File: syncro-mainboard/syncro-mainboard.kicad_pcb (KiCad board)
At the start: 4 copper layers, 78.5 x 59 mm, 146 parts, among them J1 USB_C_Receptacle_USB2.0_16P, J2 Conn_01x03, J3 Conn_ARM_JTAG_SWD_10, J4 Micro_SD_Card_Det1, J5 USB_A, J6 USB_A, J7 USB_A, J8 MikroBUS, J9 Qwiic, Q1 AO3401A, SW1 RESET, SW2 USB BOOT, SW3 SW_USER, U1 MYC-YF135, U10 ECMF02-2AMX6, U11 TPS25200, U2 TS3USB221ARSER, U3 TS3USB221ARSER, U4 ECMF02-2AMX6, U5 FE1.1s, U6 TPS25200, U7 EMIF06-MSD02N16, U8 ECMF02-2AMX6, U9 ECMF02-2AMX6, Y1 12MHz

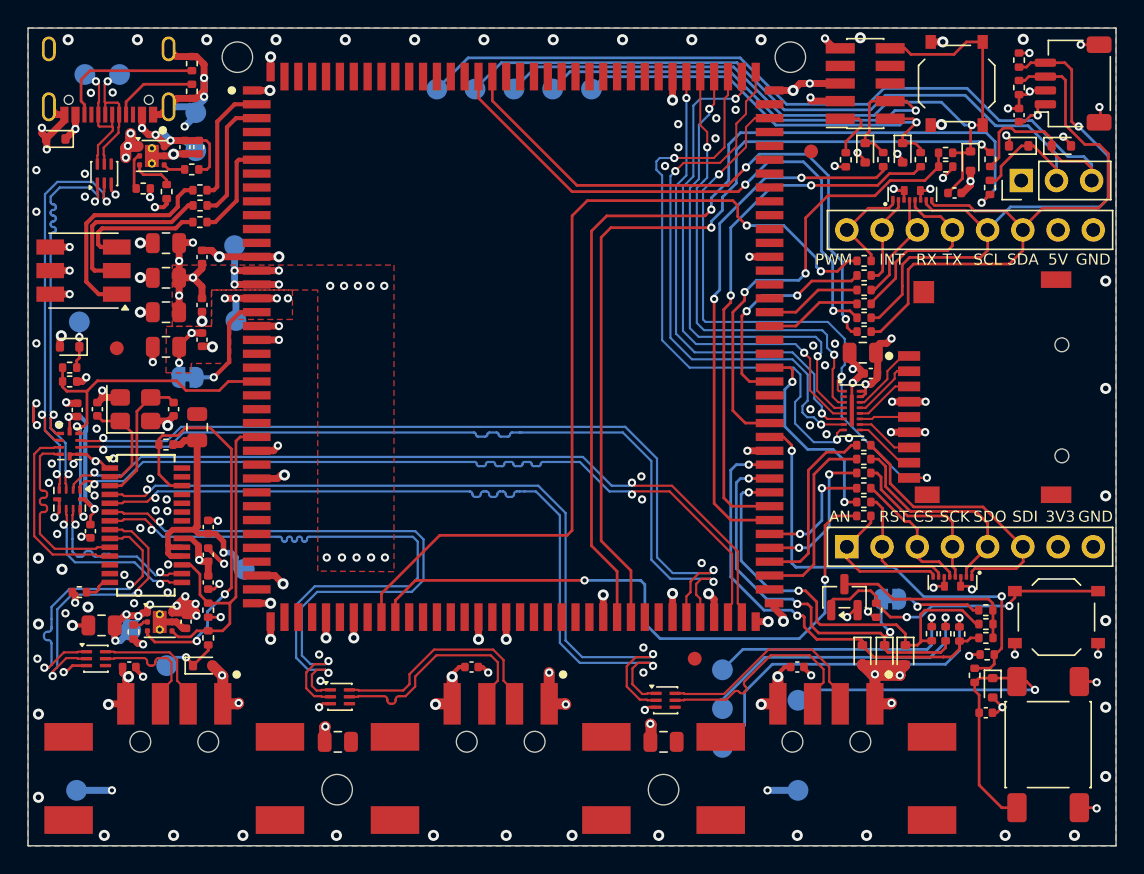
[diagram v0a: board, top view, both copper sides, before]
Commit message: Syncro mainboard rev 3
* Add XL-1615 accent RGB LEDs D16-D18 on TIM8
* Add R48-R56 next to the LEDs and rework their shared +3.3V feed
* Add In2 GND return plane under the USB-C connector for TP5/TP6
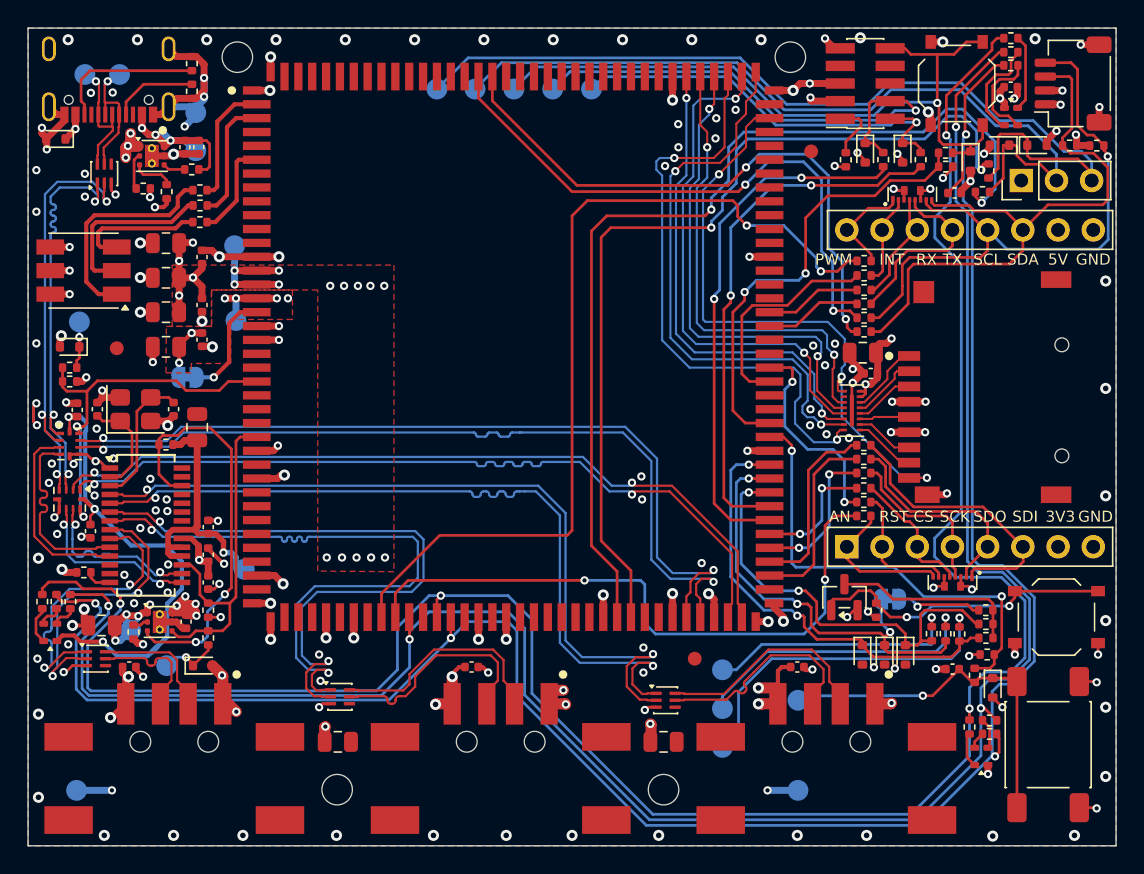
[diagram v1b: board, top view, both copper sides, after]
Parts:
- added D16: XL-1615RGBC-RF, dbl-ic:LED_RGB_XINGLIGHT_XL-1615RGBC, F.Cu at (164.6, 75.1)
- added D17: XL-1615RGBC-RF, dbl-ic:LED_RGB_XINGLIGHT_XL-1615RGBC, F.Cu at (162.5, 121.3)
- added D18: XL-1615RGBC-RF, dbl-ic:LED_RGB_XINGLIGHT_XL-1615RGBC, F.Cu at (95.3, 112.3)
- added R48: 510, Resistor_SMD:R_0402_1005Metric, F.Cu at (164.6, 69.5)
- added R49: 2.2k, Resistor_SMD:R_0402_1005Metric, F.Cu at (164.6, 71.4)
- added R50: 330, Resistor_SMD:R_0402_1005Metric, F.Cu at (164.6, 70.5)
- added R51: 510, Resistor_SMD:R_0402_1005Metric, F.Cu at (161.6, 119.2)
- added R52: 2.2k, Resistor_SMD:R_0402_1005Metric, F.Cu at (163.1, 119.7)
- added R53: 330, Resistor_SMD:R_0402_1005Metric, F.Cu at (163.1, 118.7)
- added R54: 510, Resistor_SMD:R_0402_1005Metric, F.Cu at (94.7, 110.1)
- added R55: 2.2k, Resistor_SMD:R_0402_1005Metric, F.Cu at (95.8, 110.1)
- added R56: 330, Resistor_SMD:R_0402_1005Metric, F.Cu at (96.8, 110.1)
- ? (x3): footprint Fiducial:Fiducial_1mm_Mask2mm -> dbl-mech:Fiducial_1mm_Mask2mm
- moved R47 8.34 mm to (170.8, 77.2), turned to 0 degrees
- moved R46 5.55 mm to (168.8, 77.2), turned to 180 degrees
- moved C19 3.96 mm to (160.4, 115.0), turned to 180 degrees
- moved C29 2.11 mm to (164.6, 73.0), turned to 0 degrees
- moved D5 1.76 mm to (166.5, 77.2)
- moved R7 1.46 mm to (97.7, 108.0)
- moved D4 1.39 mm to (163.8, 77.2)
- moved R15 0.84 mm to (163.0, 79.1)
- moved R16 0.63 mm to (162.6, 80.6), turned to 0 degrees
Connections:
- U1 pad 49: unconnected-(U1Spare 1-74-PB0/ETH1_RXD2-Pad49) -> /STM32MP13 SOM/LED2_B
- U1 pad 51: unconnected-(U1Spare 1-74-PB1/ETH1_RXD3-Pad51) -> /STM32MP13 SOM/LED2_R
- U1 pad 52: unconnected-(U1Spare 1-74-PA7/ETH1_RXCTL-Pad52) -> /STM32MP13 SOM/LED2_G
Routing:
- net /STM32MP13 SOM/LED2_R: track 0.00 -> 159.8 mm, vias 0 -> 4
- net /STM32MP13 SOM/LED2_B: track 0.00 -> 151.1 mm, vias 0 -> 4
- net /STM32MP13 SOM/LED2_G: track 0.00 -> 150.6 mm, vias 0 -> 4
- net +3.3V: track 58.4 -> 84.7 mm, vias 25 -> 27
- net GND: track 163.9 -> 155.3 mm, vias 176 -> 177
- net Net-(D16-BK): track 0.00 -> 7.29 mm
- net Net-(D16-GK): track 0.00 -> 6.80 mm
- net /System IO/USER_BTN_X: track 33.2 -> 27.2 mm
- net Net-(D16-RK): track 0.00 -> 5.49 mm
- net /Debug/UART4_TX: track 61.8 -> 65.6 mm
- net +5VP: track 23.9 -> 27.2 mm
- net Net-(D18-RK): track 0.00 -> 2.75 mm
- net Net-(D17-RK): track 0.00 -> 2.54 mm
- net Net-(D17-BK): track 0.00 -> 2.24 mm
- net Net-(D18-GK): track 0.00 -> 1.83 mm
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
